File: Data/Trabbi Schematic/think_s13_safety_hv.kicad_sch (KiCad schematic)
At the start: 5 parts, among them U1 Collision Control Unit (C050), U2 Contactor Box Internal Detail, U3 HV Distribution Box Detail

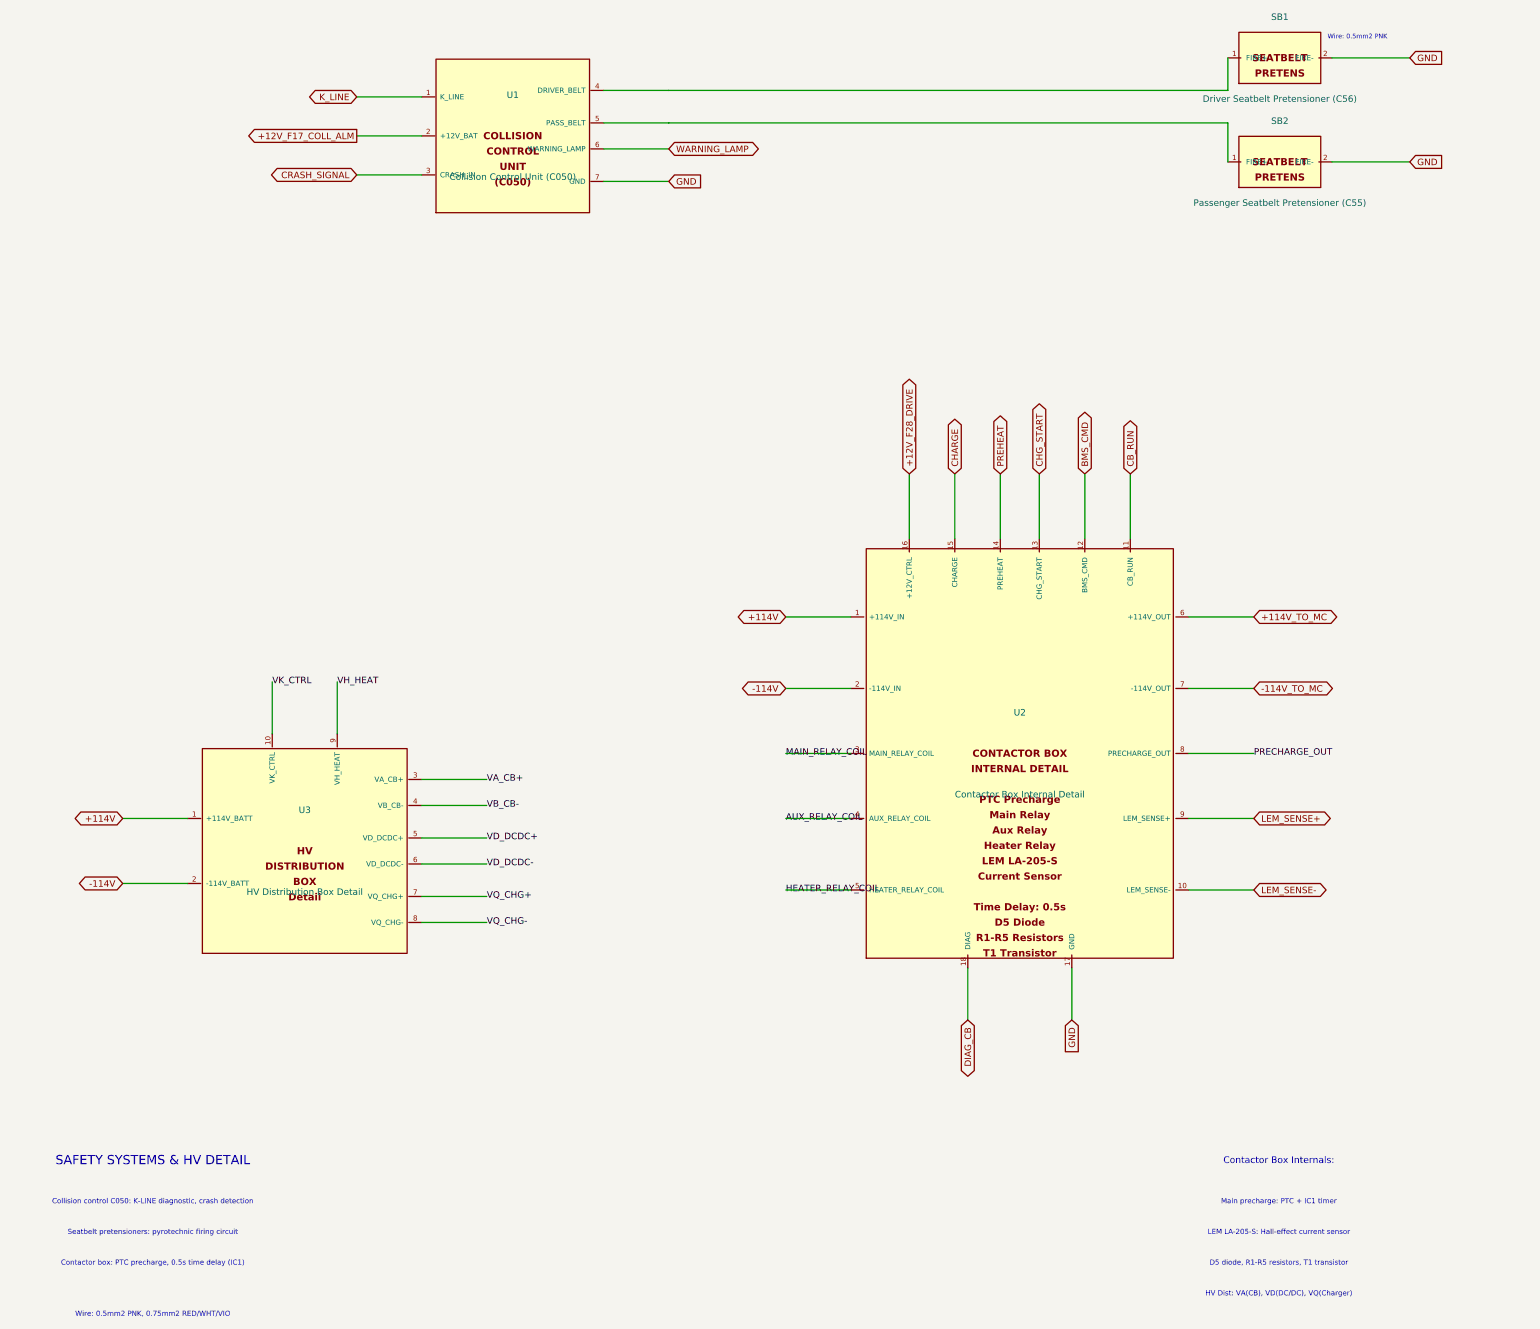
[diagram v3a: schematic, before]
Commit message: Fix label/text positioning: Ref/Value outside body, hide pin numbers
- Reference placed above body edge, Value below (dynamic based on
  symbol height) — no longer overlapping body text
- Pin numbers hidden (clutter, not useful in schematic view)
- Pin name font reduced from 1.016mm to 0.762mm (less overlap)
- Pin length increased from 2.54mm to 3.81mm (more room for pin names
  between body edge and endpoint)
- Store symbol dimensions in _sym_dims for dynamic property placement

Co-Authored-By: Claude Opus 4.6 <noreply@anthropic.com>
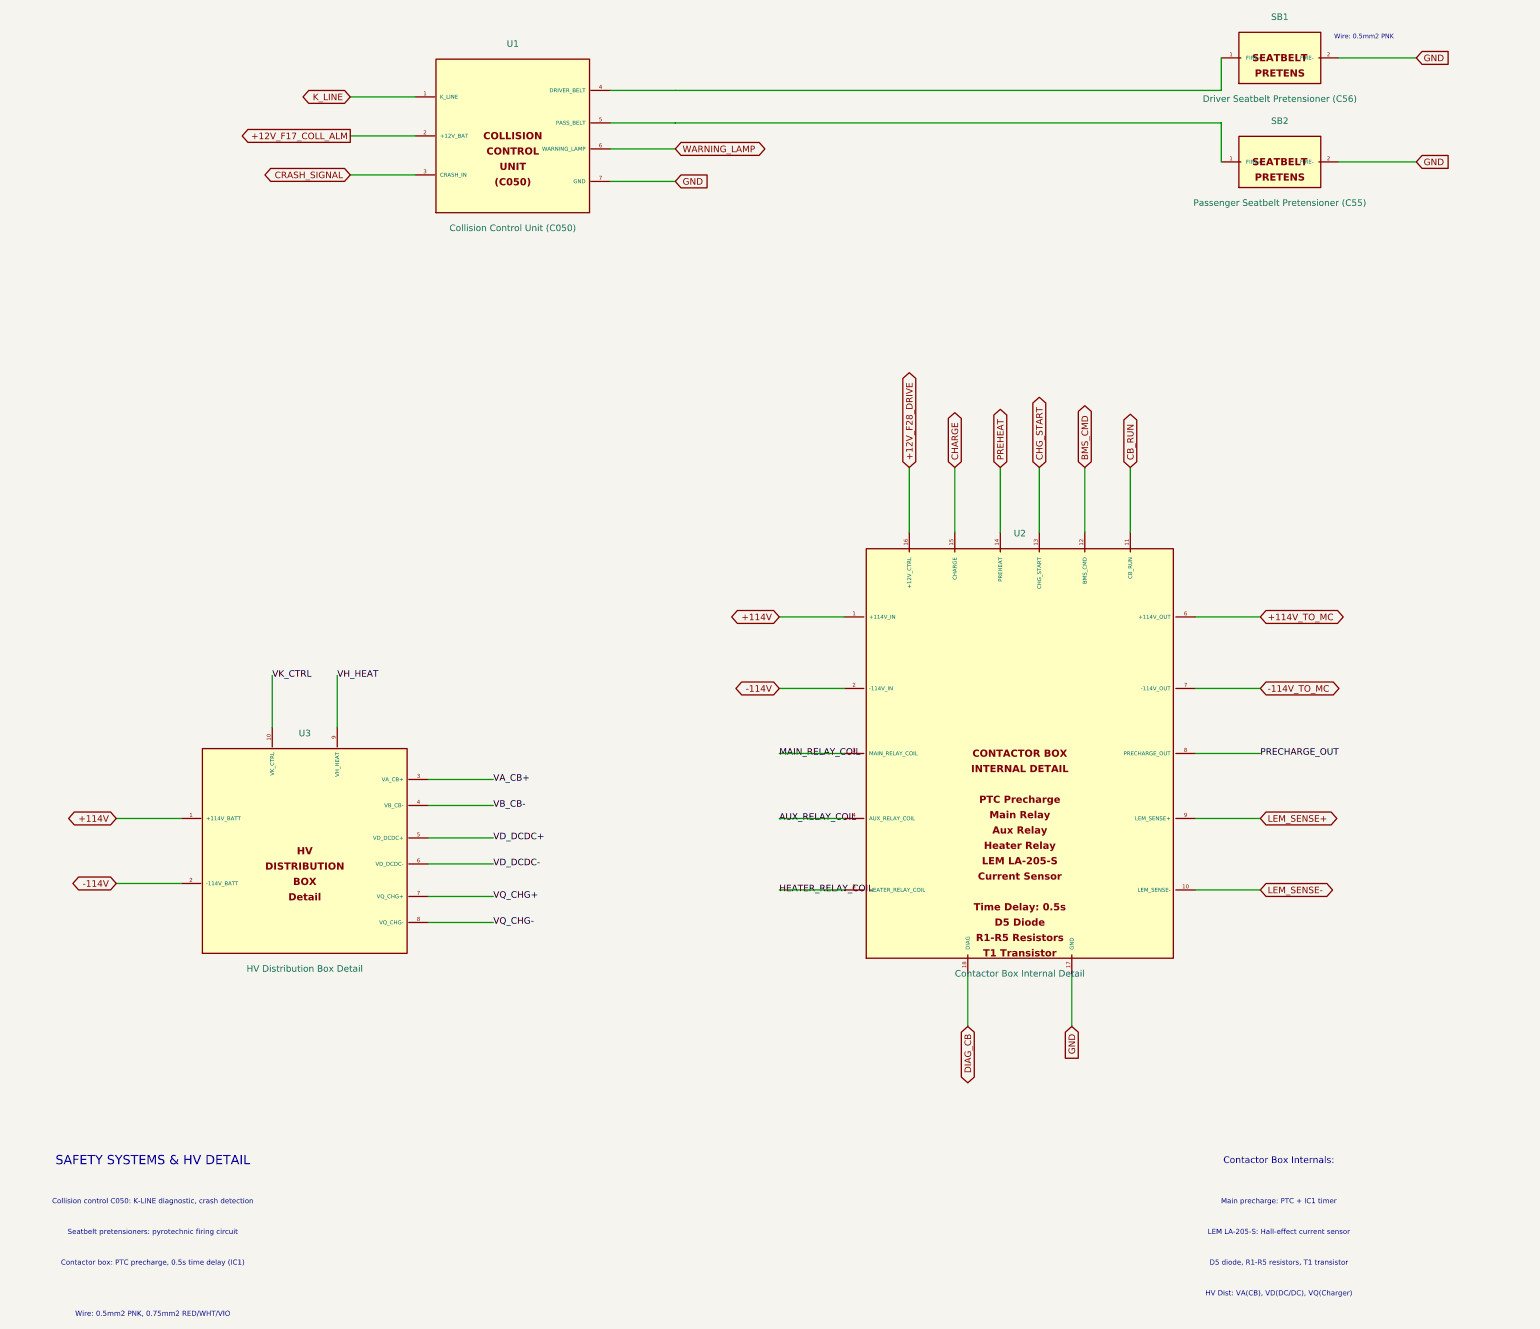
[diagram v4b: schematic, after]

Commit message: Add cross-sheet reference annotations to global labels
- Track all global label positions per sheet during build
- After building all sheets, annotate each global label with
  "→S01,S03,..." text showing which other sheets share the net
- 60 cross-sheet nets identified and annotated
- Two-pass build: 1) build all sheets 2) add cross-refs + save
- Text placed near label in 0.8mm font, offset to avoid overlap

Co-Authored-By: Claude Opus 4.6 <noreply@anthropic.com>
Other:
- note added: "→S01,S02,S03,S04,S05,S06,S07,S08,S09,S10,S11,S12"
- note added: "→S01,S02,S06"
- note added: "→S01,S07,S10,S11"
- note added: "→S02"
- note added: "→S02,S03,S06"
- note added: "→S02,S03,S06,S11"
- note added: "→S02,S05"
- note added: "→S02,S06"
- note added: "→S05"
- note added: "→S11"
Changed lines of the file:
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@@
     (effects (font (size 1.000 1.000)))
+  )
+  (text "→S02,S03,S06,S11" (at 65.580 54.570 0)
+    (effects (font (size 0.800 0.800)))
+  )
+  (text "→S01,S07,S10,S11" (at 65.580 62.190 0)
+    (effects (font (size 0.800 0.800)))
+  )
+  (text "→S11" (at 65.580 69.810 0)
+    (effects (font (size 0.800 0.800)))
+  )
+  (text "→S01,S02,S03,S04,S05,S06,S07,S08,S09,S10,S11,S12" (at 135.080 71.080 0)
+    (effects (font (size 0.800 0.800)))
+  )
+  (text "→S01,S02,S03,S04,S05,S06,S07,S08,S09,S10,S11,S12" (at 279.860 46.950 0)
+    (effects (font (size 0.800 0.800)))
+  )
+  (text "→S01,S02,S03,S04,S05,S06,S07,S08,S09,S10,S11,S12" (at 279.860 67.270 0)
+    (effects (font (size 0.800 0.800)))
+  )
+  (text "→S01,S02,S03,S04,S05,S06,S07,S08,S09,S10,S11,S12" (at 212.550 235.680 0)
+    (effects (font (size 0.800 0.800)))
+  )
+  (text "→S02,S05" (at 149.400 156.170 0)
+    (effects (font (size 0.800 0.800)))
+  )
+  (text "→S02,S05" (at 19.860 195.540 0)
+    (effects (font (size 0.800 0.800)))
+  )
+  (text "→S05" (at 149.400 170.140 0)
+    (effects (font (size 0.800 0.800)))
+  )
+  (text "→S05" (at 19.860 208.240 0)
+    (effects (font (size 0.800 0.800)))
+  )
+  (text "→S02" (at 223.980 122.460 0)
+    (effects (font (size 0.800 0.800)))
+  )
+  (text "→S02,S03,S06" (at 215.090 122.460 0)
+    (effects (font (size 0.800 0.800)))
+  )
+  (text "→S02,S06" (at 206.200 122.460 0)
+    (effects (font (size 0.800 0.800)))
+  )
+  (text "→S02" (at 198.580 122.460 0)
+    (effects (font (size 0.800 0.800)))
+  )
+  (text "→S02" (at 189.690 122.460 0)
+    (effects (font (size 0.800 0.800)))
+  )
+  (text "→S01,S02,S06" (at 180.800 122.460 0)
+    (effects (font (size 0.800 0.800)))
   )
   (symbol_instances)

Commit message: Fix label text justification for KiCad 9
Add (justify left) to all label and global_label effects.
KiCad 9 requires explicit text justification — without it,
label text is mispositioned relative to the label shape.

Co-Authored-By: Claude Opus 4.6 <noreply@anthropic.com>
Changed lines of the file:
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@@
   )
   (global_label "K_LINE" (shape bidirectional) (at 68.580 52.070 180)
-    (effects (font (size 1.27 1.27)))
+    (effects (font (size 1.27 1.27)) (justify left))
     (property "Intersheetrefs" "${INTERSHEET_REFS}" (at 68.580 52.070 0)
       (effects (font (size 1.27 1.27)) hide)
@@
   )
   (global_label "+12V_F17_COLL_ALM" (shape output) (at 68.580 59.690 180)
-    (effects (font (size 1.27 1.27)))
+    (effects (font (size 1.27 1.27)) (justify left))
     (property "Intersheetrefs" "${INTERSHEET_REFS}" (at 68.580 59.690 0)
       (effects (font (size 1.27 1.27)) hide)
@@
   )
   (global_label "CRASH_SIGNAL" (shape bidirectional) (at 68.580 67.310 180)
-    (effects (font (size 1.27 1.27)))
+    (effects (font (size 1.27 1.27)) (justify left))
     (property "Intersheetrefs" "${INTERSHEET_REFS}" (at 68.580 67.310 0)
       (effects (font (size 1.27 1.27)) hide)
@@
   )
   (global_label "WARNING_LAMP" (shape bidirectional) (at 132.080 62.230 0)
-    (effects (font (size 1.27 1.27)))
+    (effects (font (size 1.27 1.27)) (justify left))
     (property "Intersheetrefs" "${INTERSHEET_REFS}" (at 132.080 62.230 0)
       (effects (font (size 1.27 1.27)) hide)
@@
   )
   (global_label "GND" (shape input) (at 132.080 68.580 0)
-    (effects (font (size 1.27 1.27)))
+    (effects (font (size 1.27 1.27)) (justify left))
     (property "Intersheetrefs" "${INTERSHEET_REFS}" (at 132.080 68.580 0)
       (effects (font (size 1.27 1.27)) hide)
@@
   )
   (global_label "GND" (shape input) (at 276.860 44.450 0)
-    (effects (font (size 1.27 1.27)))
+    (effects (font (size 1.27 1.27)) (justify left))
     (property "Intersheetrefs" "${INTERSHEET_REFS}" (at 276.860 44.450 0)
       (effects (font (size 1.27 1.27)) hide)
@@
   )
   (global_label "GND" (shape input) (at 276.860 64.770 0)
-    (effects (font (size 1.27 1.27)))
+    (effects (font (size 1.27 1.27)) (justify left))
     (property "Intersheetrefs" "${INTERSHEET_REFS}" (at 276.860 64.770 0)
       (effects (font (size 1.27 1.27)) hide)
@@
   )
   (global_label "+114V" (shape bidirectional) (at 152.400 153.670 180)
-    (effects (font (size 1.27 1.27)))
+    (effects (font (size 1.27 1.27)) (justify left))
     (property "Intersheetrefs" "${INTERSHEET_REFS}" (at 152.400 153.670 0)
       (effects (font (size 1.27 1.27)) hide)
@@
   )
   (global_label "-114V" (shape bidirectional) (at 152.400 167.640 180)
-    (effects (font (size 1.27 1.27)))
+    (effects (font (size 1.27 1.27)) (justify left))
     (property "Intersheetrefs" "${INTERSHEET_REFS}" (at 152.400 167.640 0)
       (effects (font (size 1.27 1.27)) hide)
@@
   )
   (label "MAIN_RELAY_COIL" (at 152.400 180.340 0)
-    (effects (font (size 1.27 1.27)))
+    (effects (font (size 1.27 1.27)) (justify left))
   )
   (wire (pts (xy 165.100 193.040) (xy 152.400 193.040))
@@
   )
   (label "AUX_RELAY_COIL" (at 152.400 193.040 0)
-    (effects (font (size 1.27 1.27)))
+    (effects (font (size 1.27 1.27)) (justify left))
   )
   (wire (pts (xy 165.100 207.010) (xy 152.400 207.010))
@@
   )
   (label "HEATER_RELAY_COIL" (at 152.400 207.010 0)
-    (effects (font (size 1.27 1.27)))
+    (effects (font (size 1.27 1.27)) (justify left))
   )
   (wire (pts (xy 233.680 153.670) (xy 246.380 153.670))
@@
   )
   (global_label "+114V_TO_MC" (shape bidirectional) (at 246.380 153.670 0)
-    (effects (font (size 1.27 1.27)))
+    (effects (font (size 1.27 1.27)) (justify left))
     (property "Intersheetrefs" "${INTERSHEET_REFS}" (at 246.380 153.670 0)
       (effects (font (size 1.27 1.27)) hide)
@@
   )
   (global_label "-114V_TO_MC" (shape bidirectional) (at 246.380 167.640 0)
-    (effects (font (size 1.27 1.27)))
+    (effects (font (size 1.27 1.27)) (justify left))
     (property "Intersheetrefs" "${INTERSHEET_REFS}" (at 246.380 167.640 0)
       (effects (font (size 1.27 1.27)) hide)
@@
   )
   (label "PRECHARGE_OUT" (at 246.380 180.340 0)
-    (effects (font (size 1.27 1.27)))
+    (effects (font (size 1.27 1.27)) (justify left))
   )
   (wire (pts (xy 233.680 193.040) (xy 246.380 193.040))
@@
   )
   (global_label "LEM_SENSE+" (shape bidirectional) (at 246.380 193.040 0)
-    (effects (font (size 1.27 1.27)))
+    (effects (font (size 1.27 1.27)) (justify left))
     (property "Intersheetrefs" "${INTERSHEET_REFS}" (at 246.380 193.040 0)
       (effects (font (size 1.27 1.27)) hide)
@@
   )
   (global_label "LEM_SENSE-" (shape bidirectional) (at 246.380 207.010 0)
-    (effects (font (size 1.27 1.27)))
+    (effects (font (size 1.27 1.27)) (justify left))
     (property "Intersheetrefs" "${INTERSHEET_REFS}" (at 246.380 207.010 0)
       (effects (font (size 1.27 1.27)) hide)
@@
   )
   (global_label "CB_RUN" (shape bidirectional) (at 220.980 124.460 90)
-    (effects (font (size 1.27 1.27)))
+    (effects (font (size 1.27 1.27)) (justify left))
     (property "Intersheetrefs" "${INTERSHEET_REFS}" (at 220.980 124.460 0)
       (effects (font (size 1.27 1.27)) hide)
@@
   )
   (global_label "BMS_CMD" (shape bidirectional) (at 212.090 124.460 90)
-    (effects (font (size 1.27 1.27)))
+    (effects (font (size 1.27 1.27)) (justify left))
     (property "Intersheetrefs" "${INTERSHEET_REFS}" (at 212.090 124.460 0)
       (effects (font (size 1.27 1.27)) hide)
@@
   )
   (global_label "CHG_START" (shape bidirectional) (at 203.200 124.460 90)
-    (effects (font (size 1.27 1.27)))
+    (effects (font (size 1.27 1.27)) (justify left))
     (property "Intersheetrefs" "${INTERSHEET_REFS}" (at 203.200 124.460 0)
       (effects (font (size 1.27 1.27)) hide)
@@
   )
   (global_label "PREHEAT" (shape bidirectional) (at 195.580 124.460 90)
-    (effects (font (size 1.27 1.27)))
+    (effects (font (size 1.27 1.27)) (justify left))
     (property "Intersheetrefs" "${INTERSHEET_REFS}" (at 195.580 124.460 0)
       (effects (font (size 1.27 1.27)) hide)
@@
   )
   (global_label "CHARGE" (shape bidirectional) (at 186.690 124.460 90)
-    (effects (font (size 1.27 1.27)))
+    (effects (font (size 1.27 1.27)) (justify left))
     (property "Intersheetrefs" "${INTERSHEET_REFS}" (at 186.690 124.460 0)
       (effects (font (size 1.27 1.27)) hide)
@@
   )
   (global_label "+12V_F28_DRIVE" (shape bidirectional) (at 177.800 124.460 90)
-    (effects (font (size 1.27 1.27)))
+    (effects (font (size 1.27 1.27)) (justify left))
     (property "Intersheetrefs" "${INTERSHEET_REFS}" (at 177.800 124.460 0)
       (effects (font (size 1.27 1.27)) hide)
@@
   )
   (global_label "GND" (shape input) (at 209.550 233.680 270)
-    (effects (font (size 1.27 1.27)))
+    (effects (font (size 1.27 1.27)) (justify left))
     (property "Intersheetrefs" "${INTERSHEET_REFS}" (at 209.550 233.680 0)
       (effects (font (size 1.27 1.27)) hide)
@@
   )
   (global_label "DIAG_CB" (shape bidirectional) (at 189.230 233.680 270)
-    (effects (font (size 1.27 1.27)))
+    (effects (font (size 1.27 1.27)) (justify left))
     (property "Intersheetrefs" "${INTERSHEET_REFS}" (at 189.230 233.680 0)
       (effects (font (size 1.27 1.27)) hide)
@@
   )
   (global_label "+114V" (shape bidirectional) (at 22.860 193.040 180)
-    (effects (font (size 1.27 1.27)))
+    (effects (font (size 1.27 1.27)) (justify left))
     (property "Intersheetrefs" "${INTERSHEET_REFS}" (at 22.860 193.040 0)
       (effects (font (size 1.27 1.27)) hide)
@@
   )
   (global_label "-114V" (shape bidirectional) (at 22.860 205.740 180)
-    (effects (font (size 1.27 1.27)))
+    (effects (font (size 1.27 1.27)) (justify left))
     (property "Intersheetrefs" "${INTERSHEET_REFS}" (at 22.860 205.740 0)
       (effects (font (size 1.27 1.27)) hide)
@@
   )
   (label "VA_CB+" (at 96.520 185.420 0)
-    (effects (font (size 1.27 1.27)))
+    (effects (font (size 1.27 1.27)) (justify left))
   )
   (wire (pts (xy 83.820 190.500) (xy 96.520 190.500))
@@
   )
   (label "VB_CB-" (at 96.520 190.500 0)
-    (effects (font (size 1.27 1.27)))
+    (effects (font (size 1.27 1.27)) (justify left))
   )
   (wire (pts (xy 83.820 196.850) (xy 96.520 196.850))
@@
   )
   (label "VD_DCDC+" (at 96.520 196.850 0)
-    (effects (font (size 1.27 1.27)))
+    (effects (font (size 1.27 1.27)) (justify left))
   )
   (wire (pts (xy 83.820 201.930) (xy 96.520 201.930))
@@
   )
   (label "VD_DCDC-" (at 96.520 201.930 0)
-    (effects (font (size 1.27 1.27)))
+    (effects (font (size 1.27 1.27)) (justify left))
   )
   (wire (pts (xy 83.820 208.280) (xy 96.520 208.280))
@@
   )
   (label "VQ_CHG+" (at 96.520 208.280 0)
-    (effects (font (size 1.27 1.27)))
+    (effects (font (size 1.27 1.27)) (justify left))
   )
   (wire (pts (xy 83.820 213.360) (xy 96.520 213.360))
@@
   )
   (label "VQ_CHG-" (at 96.520 213.360 0)
-    (effects (font (size 1.27 1.27)))
+    (effects (font (size 1.27 1.27)) (justify left))
   )
   (wire (pts (xy 66.040 175.260) (xy 66.040 165.100))
@@
   )
   (label "VH_HEAT" (at 66.040 165.100 0)
-    (effects (font (size 1.27 1.27)))
+    (effects (font (size 1.27 1.27)) (justify left))
   )
   (wire (pts (xy 53.340 175.260) (xy 53.340 165.100))
@@
   )
   (label "VK_CTRL" (at 53.340 165.100 0)
-    (effects (font (size 1.27 1.27)))
+    (effects (font (size 1.27 1.27)) (justify left))
   )
   (text "SAFETY SYSTEMS & HV DETAIL" (at 30.000 260.000 0)
